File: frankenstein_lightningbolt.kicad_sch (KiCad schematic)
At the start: 0 parts

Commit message: Initial schematic
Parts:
- added C1, C2: 22uF 25V 1206 RoHS, easyeda2kicad:C1206, symbol easyeda2kicad:CL31A226KAHNNNE
- added C3, C4, C6: 1uF 50V 1206 RoHS, easyeda2kicad:C1206, symbol easyeda2kicad:CL31B105KBHNNNE
- added C5: 100nF 50V 1206 RoHS, easyeda2kicad:C1206, symbol easyeda2kicad:CL31B104KBCNNNC
- added D1: SMF05CT1G, easyeda2kicad:SOT-363_L2.0-W1.3-P0.65-LS2.1-BR, symbol easyeda2kicad:SMF05CT1G
- added J1: 12V OUT, symbol Connector:Conn_01x02_Pin
- added J2: 3V3 OUT, symbol Connector:Conn_01x02_Pin
- added J3: 5V OUT, symbol Connector:Conn_01x02_Pin
- added Q1, Q2: DMP3013SFV-7, easyeda2kicad:POWERPAK-1212-8_L3.1-W3.1-P0.65-LS3.3-BL, symbol easyeda2kicad:DMP3013SFV-7
- added R1: 1KOhms ±1% 1/4W 1206 RoHS, easyeda2kicad:R1206, symbol easyeda2kicad:1206W4F1001T5E
- added R2: 10KOhms 1206, easyeda2kicad:R1206, symbol easyeda2kicad:1206W4F1002T5E
- added R3: 47KOhms ±1% 1/8W 0805 RoHS, easyeda2kicad:R0805, symbol easyeda2kicad:0805W8F4702T5E
- added R4, R6, R8: 5.1k 0603, easyeda2kicad:R0603, symbol easyeda2kicad:0603WAF5101T5E
- added R5, R7: 2.4k 0603, easyeda2kicad:R0603, symbol easyeda2kicad:0603WAF2401T5E
- added R9: 10k 0603, easyeda2kicad:R0603, symbol easyeda2kicad:0603WAF5103T5E
- added U1: CYPD3177-24LQXQ, easyeda2kicad:TQFN-24_L4.0-W4.0-P0.50-TL-EP2.8, symbol easyeda2kicad:CYPD3177-24LQXQ
- added U2: AMS1117-3.3, easyeda2kicad:SOT-223-3_L6.5-W3.4-P2.30-LS7.0-BR, symbol easyeda2kicad:AMS1117-3.3
- added U3: AMS1117-5.0, easyeda2kicad:SOT-223_L6.5-W3.5-P2.30-LS7.0-BR, symbol easyeda2kicad:AMS1117-5.0
- added USB1: AF10.0 Aparagraph After the two feet Boundless ir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, easyeda2kicad:USB-A-SMD_JTJ-USB-AF-10.0-023, symbol easyeda2kicad:AF10.0AparagraphAfterthetwofeetBoundlessironLCPVinyl6.3SMT
- added USBC1: USB3.1C16PFSMT, easyeda2kicad:USB-C-SMD_TYPE-C-USB-17, symbol easyeda2kicad:USB3.1C16PFSMT
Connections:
- new net: Q1.1 (S), Q1.2 (S), Q1.3 (S), Q2.1 (S), Q2.2 (S), Q2.3 (S), R3.2
- new net: C3.2, U1.24 (VCCD)
- new net: R1.2, U1.3 (VBUS_FET_EN)
- new net +3V3: C2.1, J2.2 (Pin_2), U2.2 (VOUT), U2.4 (VOUT)
- new net +5V: C1.1, J3.2 (Pin_2), U3.2 (VOUT), U3.4 (VOUT), USB1.1 (VCC)
- new net CC1: U1.15 (CC1), USBC1.A5 (CC1)
- new net CC2: U1.14 (CC2), USBC1.B5 (CC2)
- new net GND: C1.2, C2.2, C3.1, C4.1, C5.2, D1.2, J1.1 (Pin_1), J2.1 (Pin_1), J3.1 (Pin_1), R5.2, R7.2, R9.2, U1.19 (GND), U1.22 (GND), U1.25 (EP), U1.6 (ISNK_FINE), U2.1 (GND), U3.1 (GND), USB1.4 (GND), USBC1.A1 (GND), USBC1.A12 (GND)
- new net ISNK_COARSE: R8.2, R9.1, U1.5 (ISNK_COARSE)
- new net USB+: D1.5, USB1.3 (D+), USBC1.A6 (DP1), USBC1.B6 (DP2)
- new net USB-: D1.4, USB1.2 (D-), USBC1.A7 (DN1), USBC1.B7 (DN2)
- new net VBUS: C6.1, D1.6, Q1.5 (D), Q1.6 (D), Q1.7 (D), Q1.8 (D), R2.1, U1.18 (VBUS_IN), USBC1.A4 (VBUS), USBC1.A9 (VBUS)
- new net VBUS_FET_EN: C6.2, Q1.4 (G), Q2.4 (G), R1.1, R2.2, R3.1
- new net VBUS_MAX: R4.2, R5.1, U1.2 (VBUS_MAX)
- new net VBUS_MIN: R6.2, R7.1, U1.1 (VBUS_MIN)
- new net VDDD: C4.2, C5.1, R4.1, R6.1, R8.1, U1.23 (VDDD)
- new net Vdrive: J1.2 (Pin_2), Q2.5 (D), Q2.6 (D), Q2.7 (D), Q2.8 (D), U1.11 (VDC_OUT), U2.3 (VIN), U3.3 (VIN)
- no-connect marks 0 -> 15
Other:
- note added: "5.1k PullUp, 10k PullDown -> 4A"
- note added: "5.1k PullUp, 2.4k PullDown -> 12V"

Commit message: Fix Part IDs and missing footprints
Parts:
- J1, J2, J3: footprint (none) -> Connector_PinHeader_2.54mm:PinHeader_1x02_P2.54mm_Vertical
- U1: LCSC Part C1521054 -> C2959321
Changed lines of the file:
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@@
       (effects (font (size 1.27 1.27)) hide)
     )
-    (property "LCSC Part" "C1521054" (at 161.925 100.33 0)
+    (property "LCSC Part" "C2959321" (at 161.925 100.33 0)
       (effects (font (size 1.27 1.27)) hide)
     )
@@
       (effects (font (size 1.27 1.27)) (justify right))
     )
-    (property "Footprint" "" (at 272.415 160.655 0)
+    (property "Footprint" "Connector_PinHeader_2.54mm:PinHeader_1x02_P2.54mm_Vertical" (at 272.415 160.655 0)
       (effects (font (size 1.27 1.27)) hide)
     )
@@
       (effects (font (size 1.27 1.27)) (justify right))
     )
-    (property "Footprint" "" (at 272.415 144.145 0)
+    (property "Footprint" "Connector_PinHeader_2.54mm:PinHeader_1x02_P2.54mm_Vertical" (at 272.415 144.145 0)
       (effects (font (size 1.27 1.27)) hide)
     )
@@
       (effects (font (size 1.27 1.27)) (justify right))
     )
-    (property "Footprint" "" (at 272.415 151.765 0)
-      (effects (font (size 1.27 1.27)) hide)
-    )
+    (property "Footprint" "Connector_PinHeader_2.54mm:PinHeader_1x02_P2.54mm_Vertical" (at 272.415 151.765 0)
+      (effects (font (size 1.27 1.27)) hide)
+    )

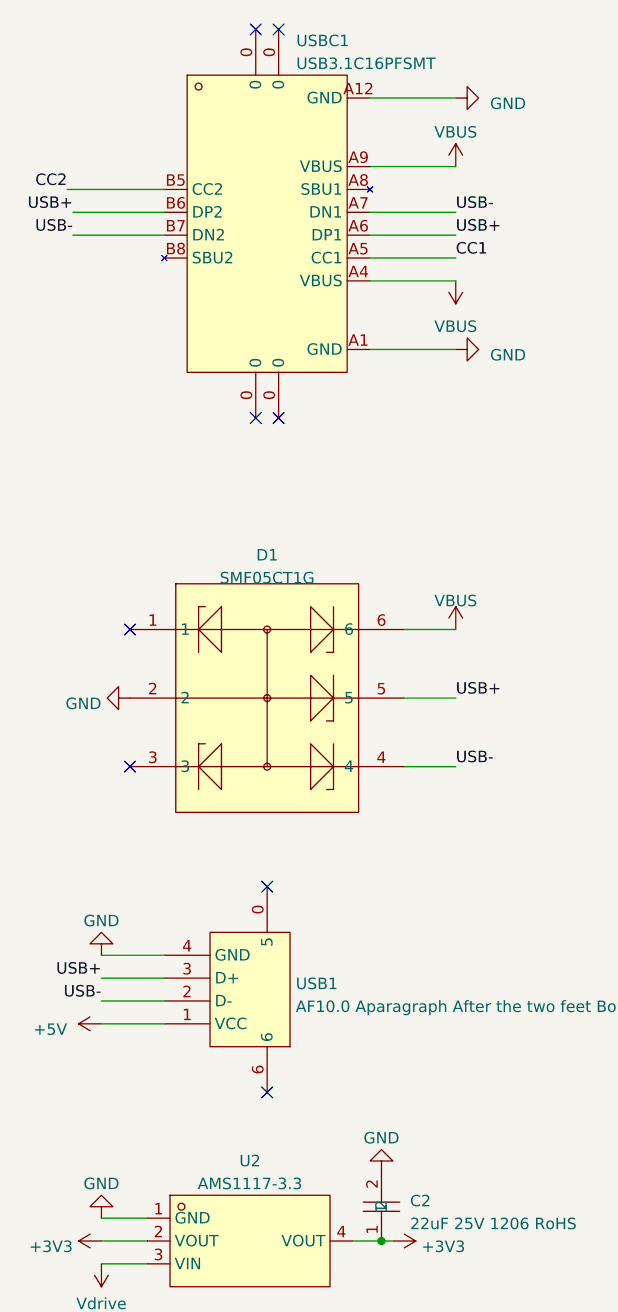
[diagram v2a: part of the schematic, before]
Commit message: Add GND to usb connectors
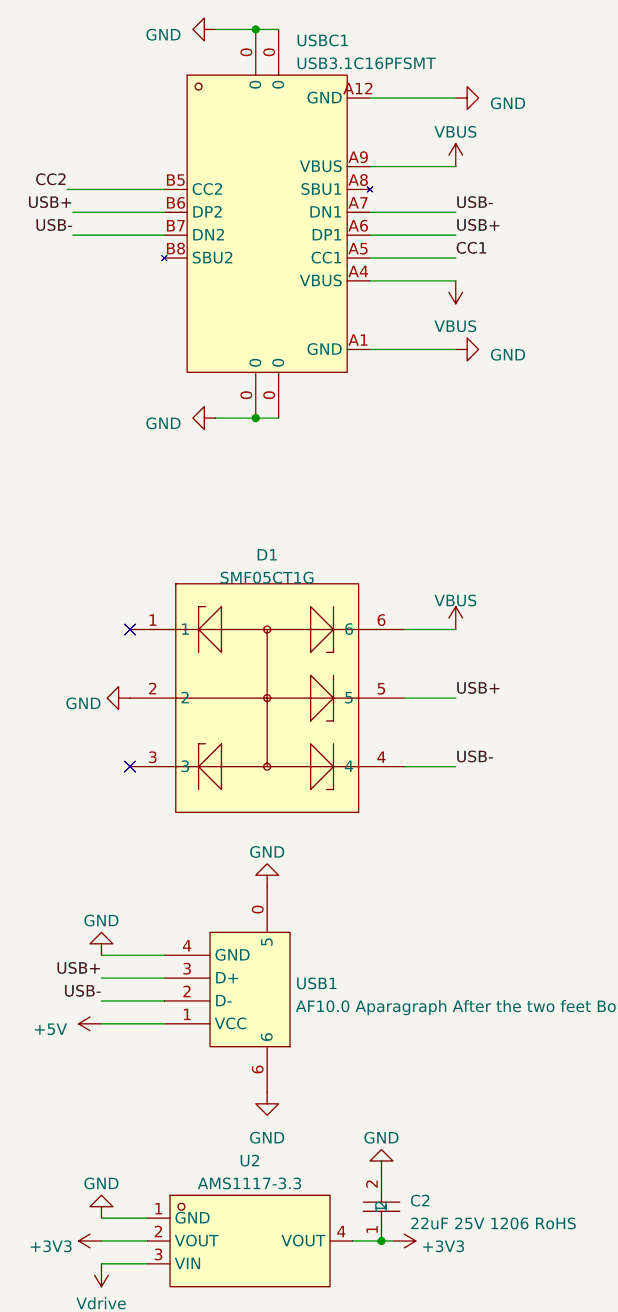
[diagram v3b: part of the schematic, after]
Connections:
- net GND: now also USB1.0 (5), USB1.6, USBC1.0
- no-connect marks 15 -> 9
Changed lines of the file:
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@@
   (junction (at 196.215 116.84) (diameter 0) (color 0 0 0 0)
   )
+  (junction (at 42.545 58.42) (diameter 0) (color 0 0 0 0)
+  )
   (junction (at 179.705 146.685) (diameter 0) (color 0 0 0 0)
   )
@@
   (junction (at 116.84 21.59) (diameter 0) (color 0 0 0 0)
   )
+  (junction (at 42.545 15.24) (diameter 0) (color 0 0 0 0)
+  )
   (junction (at 163.83 134.62) (diameter 0) (color 0 0 0 0)
   )
   (no_connect (at 141.605 74.93))
-  (no_connect (at 42.545 15.24))
-  (no_connect (at 42.545 58.42))
-  (no_connect (at 43.815 110.49))
   (no_connect (at 141.605 67.31))
   (no_connect (at 141.605 80.01))
   (no_connect (at 141.605 82.55))
   (no_connect (at 28.575 97.155))
-  (no_connect (at 45.085 15.24))
   (no_connect (at 182.245 87.63))
-  (no_connect (at 45.085 58.42))
-  (no_connect (at 43.815 133.35))
   (no_connect (at 141.605 77.47))
   (no_connect (at 141.605 87.63))
@@
     (stroke (width 0) (type default))
   )
+  (wire (pts (xy 42.545 15.24) (xy 45.085 15.24))
+    (stroke (width 0) (type default))
+  )
   (wire (pts (xy 201.295 110.49) (xy 201.295 116.84))
     (stroke (width 0) (type default))
@@
     (stroke (width 0) (type default))
   )
+  (wire (pts (xy 38.1 15.24) (xy 42.545 15.24))
+    (stroke (width 0) (type default))
+  )
   (wire (pts (xy 127 39.37) (xy 142.24 39.37))
     (stroke (width 0) (type default))
@@
     (stroke (width 0) (type default))
   )
+  (wire (pts (xy 38.1 58.42) (xy 42.545 58.42))
+    (stroke (width 0) (type default))
+  )
   (wire (pts (xy 163.83 134.62) (xy 166.37 134.62))
     (stroke (width 0) (type default))
@@
   )
   (wire (pts (xy 25.4 147.32) (xy 30.48 147.32))
+    (stroke (width 0) (type default))
+  )
+  (wire (pts (xy 42.545 58.42) (xy 45.085 58.42))
     (stroke (width 0) (type default))
   )
@@
         (path "/d1174e51-bd9a-4e44-96bb-93de6188f28e"
           (reference "#PWR025") (unit 1)
+        )
+      )
+    )
+  )
+  (symbol (lib_id "power:GND") (at 43.815 133.35 0) (unit 1)
+    (in_bom yes) (on_board yes) (dnp no) (fields_autoplaced)
+    (property "Reference" "#PWR037" (at 43.815 139.7 0)
+      (effects (font (size 1.27 1.27)) hide)
+    )
+    (property "Value" "GND" (at 43.815 138.43 0)
+      (effects (font (size 1.27 1.27)))
+    )
+    (property "Footprint" "" (at 43.815 133.35 0)
+      (effects (font (size 1.27 1.27)) hide)
+    )
+    (property "Datasheet" "" (at 43.815 133.35 0)
+      (effects (font (size 1.27 1.27)) hide)
+    )
+    (pin "1")
+    (instances
+      (project "frankenstein_lightningbolt"
+        (path "/d1174e51-bd9a-4e44-96bb-93de6188f28e"
+          (reference "#PWR037") (unit 1)
         )
       )
@@
     )
   )
+  (symbol (lib_id "power:GND") (at 38.1 58.42 270) (unit 1)
+    (in_bom yes) (on_board yes) (dnp no) (fields_autoplaced)
+    (property "Reference" "#PWR035" (at 31.75 58.42 0)
+      (effects (font (size 1.27 1.27)) hide)
+    )
+    (property "Value" "GND" (at 34.29 59.055 90)
+      (effects (font (size 1.27 1.27)) (justify right))
+    )
+    (property "Footprint" "" (at 38.1 58.42 0)
+      (effects (font (size 1.27 1.27)) hide)
+    )
+    (property "Datasheet" "" (at 38.1 58.42 0)
+      (effects (font (size 1.27 1.27)) hide)
+    )
+    (pin "1")
+    (instances
+      (project "frankenstein_lightningbolt"
+        (path "/d1174e51-bd9a-4e44-96bb-93de6188f28e"
+          (reference "#PWR035") (unit 1)
+        )
+      )
+    )
+  )
   (symbol (lib_id "power:GND") (at 56.515 165.735 180) (unit 1)
     (in_bom yes) (on_board yes) (dnp no) (fields_autoplaced)
@@
     )
   )
+  (symbol (lib_id "power:GND") (at 38.1 15.24 270) (unit 1)
+    (in_bom yes) (on_board yes) (dnp no) (fields_autoplaced)
+    (property "Reference" "#PWR036" (at 31.75 15.24 0)
+      (effects (font (size 1.27 1.27)) hide)
+    )
+    (property "Value" "GND" (at 34.29 15.875 90)
+      (effects (font (size 1.27 1.27)) (justify right))
+    )
+    (property "Footprint" "" (at 38.1 15.24 0)
+      (effects (font (size 1.27 1.27)) hide)
+    )
+    (property "Datasheet" "" (at 38.1 15.24 0)
+      (effects (font (size 1.27 1.27)) hide)
+    )
+    (pin "1")
+    (instances
+      (project "frankenstein_lightningbolt"
+        (path "/d1174e51-bd9a-4e44-96bb-93de6188f28e"
+          (reference "#PWR036") (unit 1)
+        )
+      )
+    )
+  )
   (symbol (lib_id "power:VBUS") (at 64.77 30.48 0) (unit 1)
     (in_bom yes) (on_board yes) (dnp no) (fields_autoplaced)
@@
         )
       )
+    )
+  )
+  (symbol (lib_id "power:GND") (at 43.815 110.49 180) (unit 1)
+    (in_bom yes) (on_board yes) (dnp no) (fields_autoplaced)
+    (property "Reference" "#PWR038" (at 43.815 104.14 0)
+      (effects (font (size 1.27 1.27)) hide)
+    )
+    (property "Value" "GND" (at 43.815 106.68 0)
+      (effects (font (size 1.27 1.27)))
+    )
+    (property "Footprint" "" (at 43.815 110.49 0)
+      (effects (font (size 1.27 1.27)) hide)
+    )
+    (property "Datasheet" "" (at 43.815 110.49 0)
+      (effects (font (size 1.27 1.27)) hide)
+    )
+    (pin "1")
+    (instances
+      (project "frankenstein_lightningbolt"
+        (path "/d1174e51-bd9a-4e44-96bb-93de6188f28e"
+          (reference "#PWR038") (unit 1)
+        )
+      )
